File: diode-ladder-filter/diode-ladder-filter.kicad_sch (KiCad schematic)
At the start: 67 parts, among them J1 Input, J2 CV1, J3 CV2, J4 Output, J5 Power, J6 Power, J7 Power, SW1 LPF, SW2 Resonance_safety, SW3 BPF, SW4 HPF, U1 TL074, U2 TL074

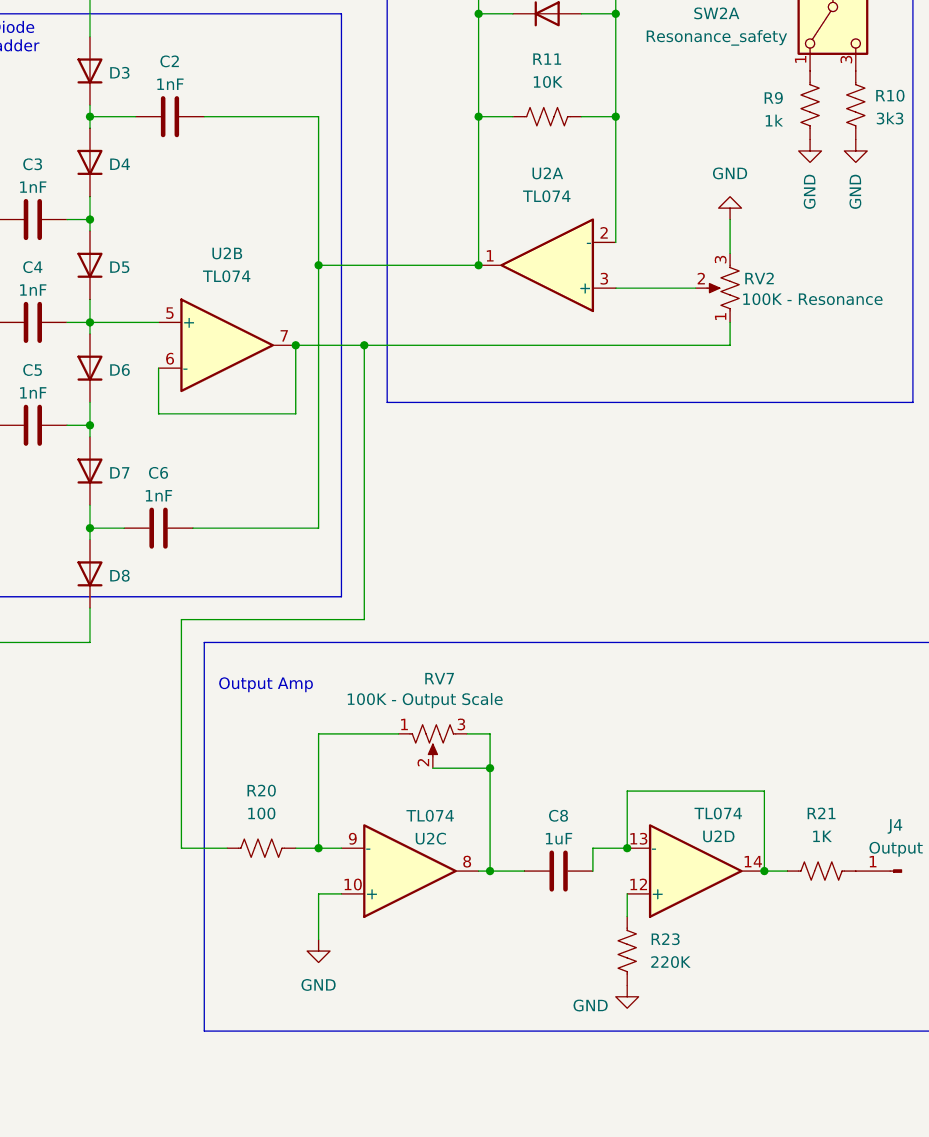
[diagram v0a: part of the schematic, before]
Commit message: Update diode ladder
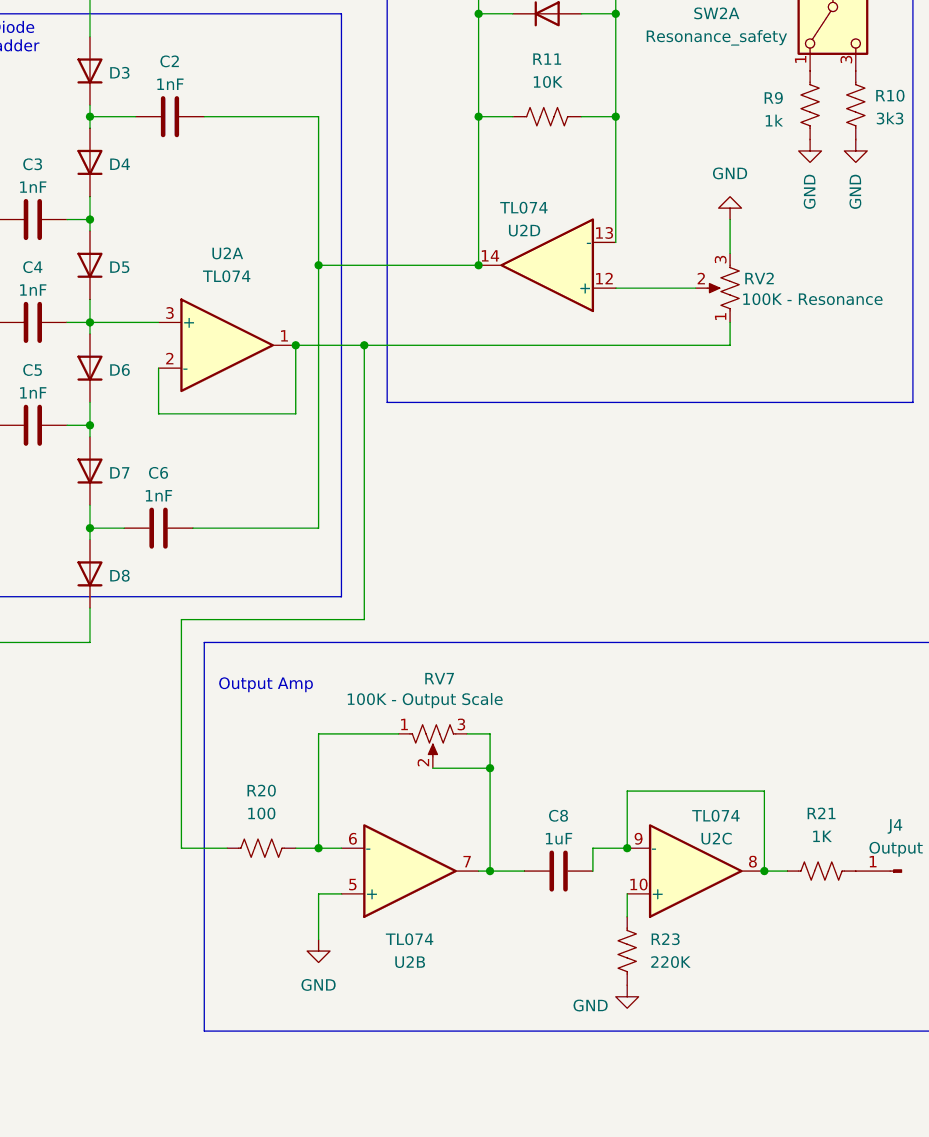
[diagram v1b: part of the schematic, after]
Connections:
- net GND: now also U2.5 (+); no longer U2.10 (+)
- net at C8.1, RV7.2, RV7.3: now also U2.7; no longer U2.8
- net at C8.2, R21.1: now also U2.8, U2.9 (-); no longer U2.13 (-), U2.14
- net at C2.2, C6.2, D1.2 (A)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: now also U2.14; no longer U2.1
- net at D1.1 (K), D2.2 (A), R11.2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: now also U2.13 (-); no longer U2.2 (-)
- net at U2.3 (+): now also C4.2, D5.1 (K), D6.2 (A); no longer RV2.2
- net at R20.2, RV7.1: now also U2.6 (-); no longer U2.9 (-)
- net at R20.1, RV2.1: now also U2.1, U2.2 (-); no longer U2.6 (-), U2.7
- net at U2.12 (+): now also RV2.2; no longer R23.1
- new net: R23.1, U2.10 (+)

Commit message: Update some modules
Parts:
- added J10: Input, modular2:banana-jack, symbol Connector:Conn_01x01_Pin
- added J11: Output, modular2:banana-jack, symbol Connector:Conn_01x01_Pin
- added J12: Conn_01x04_Socket, Connector_PinSocket_2.54mm:PinSocket_1x04_P2.54mm_Vertical, symbol Connector:Conn_01x04_Socket
- added J13: Conn_01x04_Pin, Connector_PinHeader_2.54mm:PinHeader_1x04_P2.54mm_Vertical, symbol Connector:Conn_01x04_Pin
- added J8: CV1, modular2:banana-jack, symbol Connector:Conn_01x01_Pin
- added J9: CV2, modular2:banana-jack, symbol Connector:Conn_01x01_Pin
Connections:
- net at J3.1 (Pin_1), RV4.3: now also J12.2 (Pin_2)
- net at J4.1 (Pin_1), R21.2: now also J12.4 (Pin_4)
- net at J2.1 (Pin_1), RV3.3: now also J12.1 (Pin_1)
- net at J1.1 (Pin_1), RV1.3: now also J12.3 (Pin_3)
- new net: J10.1 (Pin_1), J13.3 (Pin_3)
- new net: J13.1 (Pin_1), J8.1 (Pin_1)
- new net: J11.1 (Pin_1), J13.4 (Pin_4)
- new net: J13.2 (Pin_2), J9.1 (Pin_1)

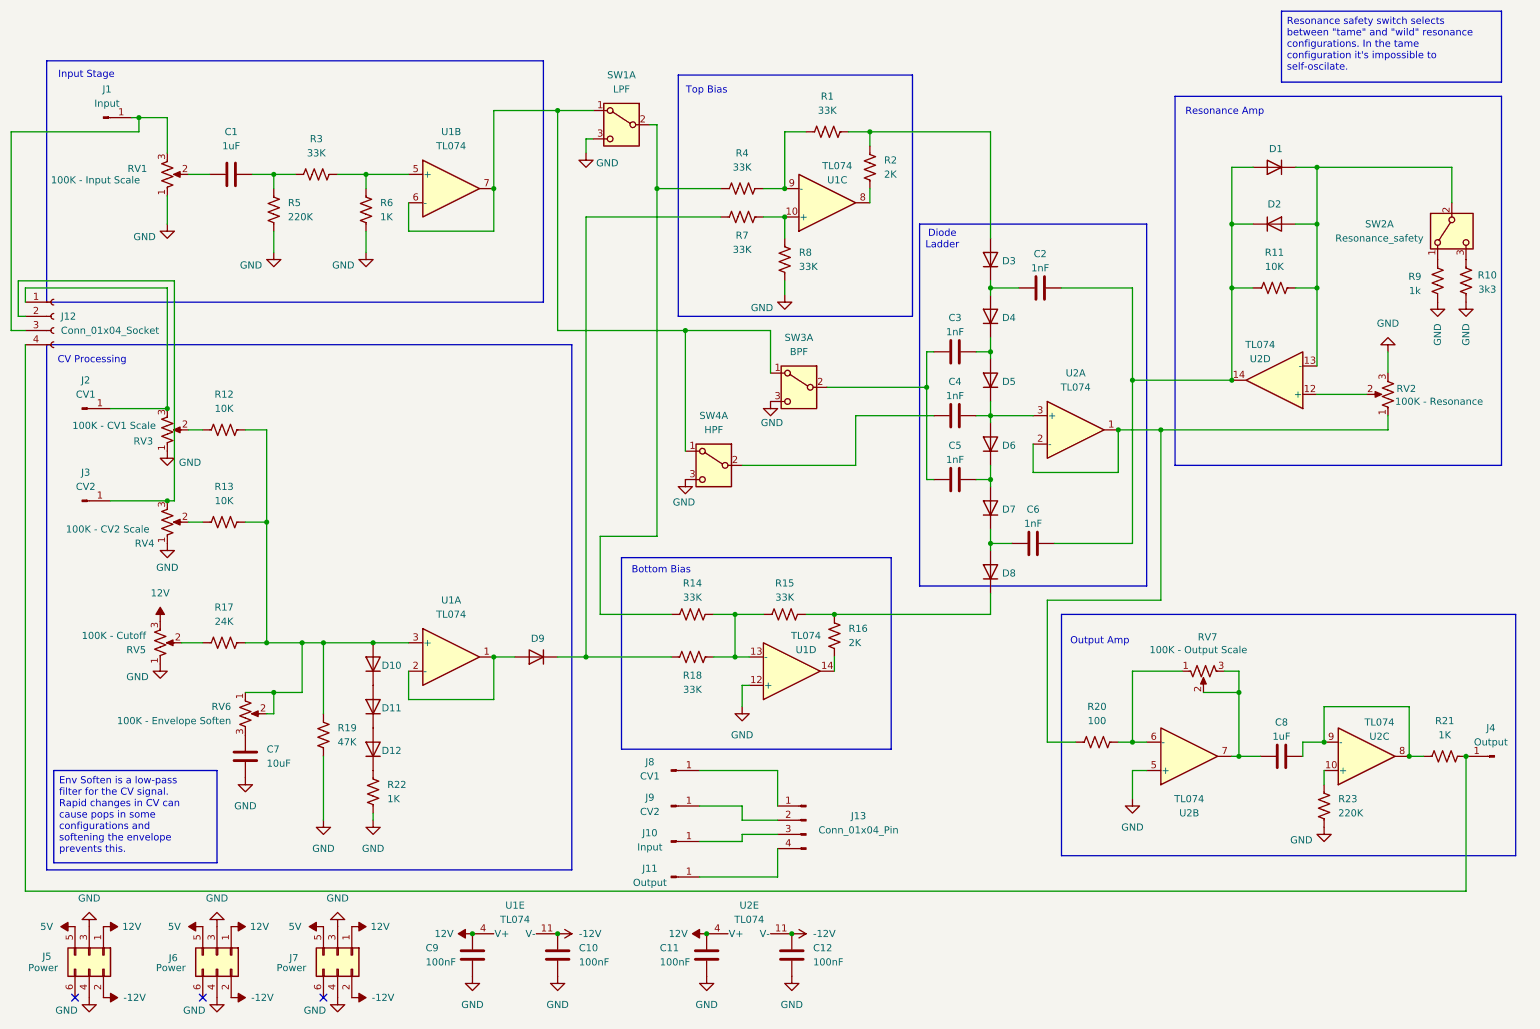
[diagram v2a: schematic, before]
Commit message: Start fixing issues with diode ladder
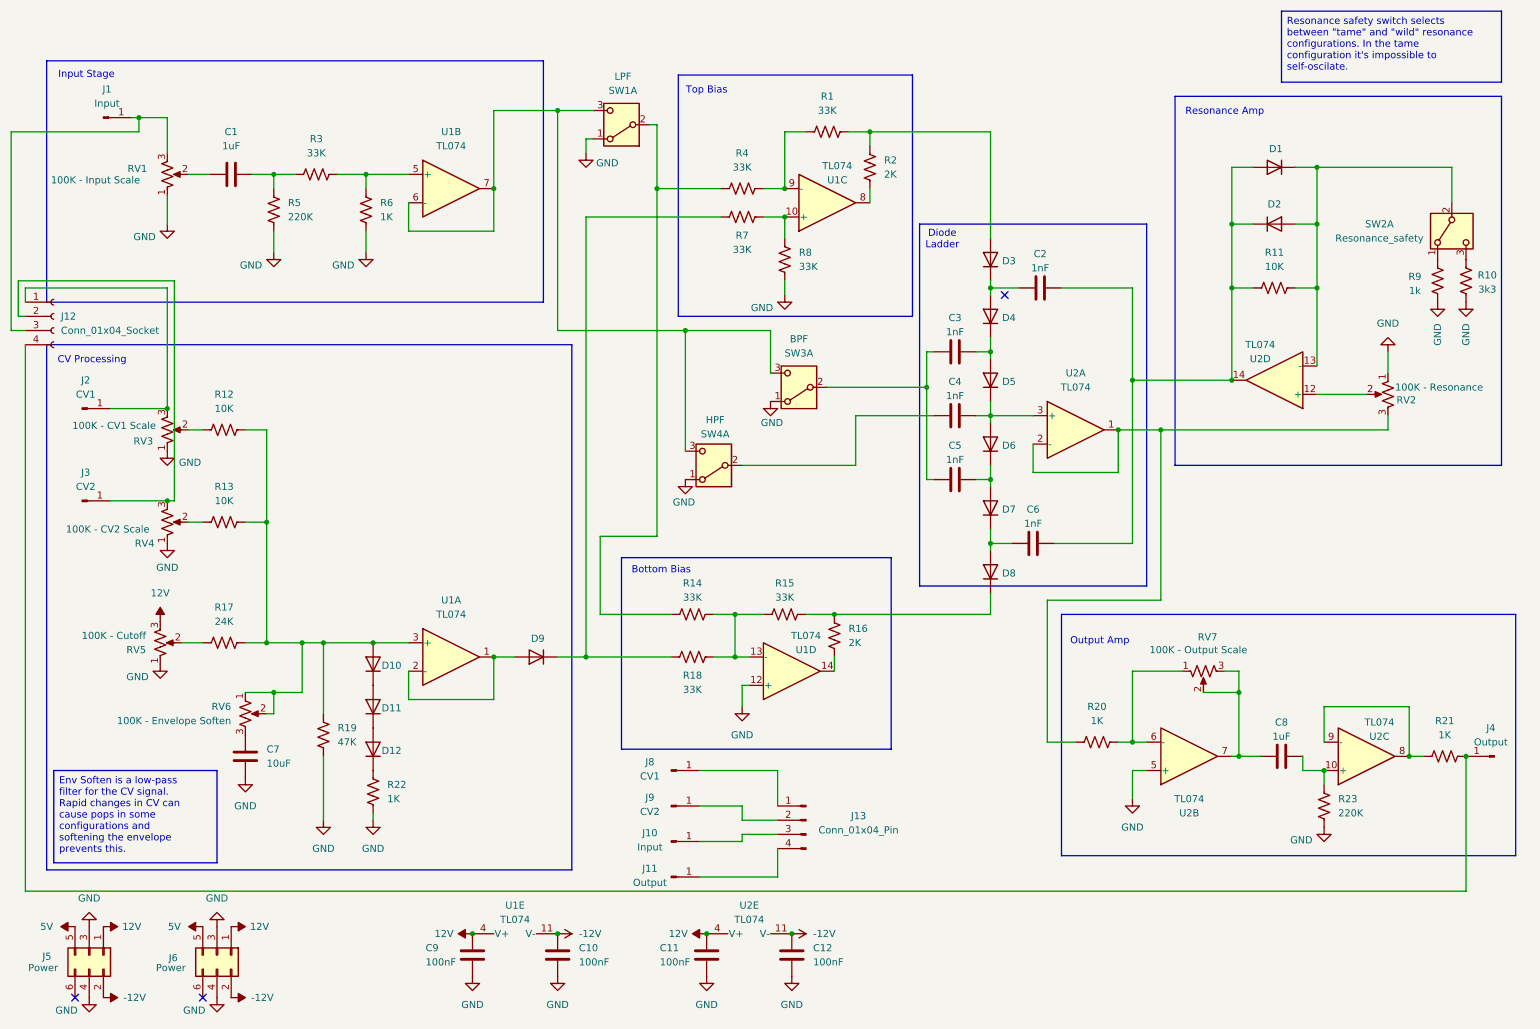
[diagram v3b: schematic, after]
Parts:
- removed J7: Power, Connector_IDC:IDC-Header_2x03_P2.54mm_Vertical, symbol Connector_Generic:Conn_02x03_Odd_Even
- R20: value 100 -> 1K
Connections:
- net GND: now also RV2.1, SW1.1 (A), SW3.1 (A), SW4.1 (A); no longer RV2.3, SW1.3 (C), SW3.3 (C), SW4.3 (C)
- net at R21.1, U2.8, U2.9 (-): no longer C8.2
- net at R20.1, U2.1, U2.2 (-): now also RV2.3; no longer RV2.1
- net at R23.1, U2.10 (+): now also C8.2
- new net: SW1.3 (C), SW3.3 (C), SW4.3 (C), U1.6 (-), U1.7
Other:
- moved on the sheet: RV2, SW1A, SW3A, SW4A

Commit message: Renumber some components
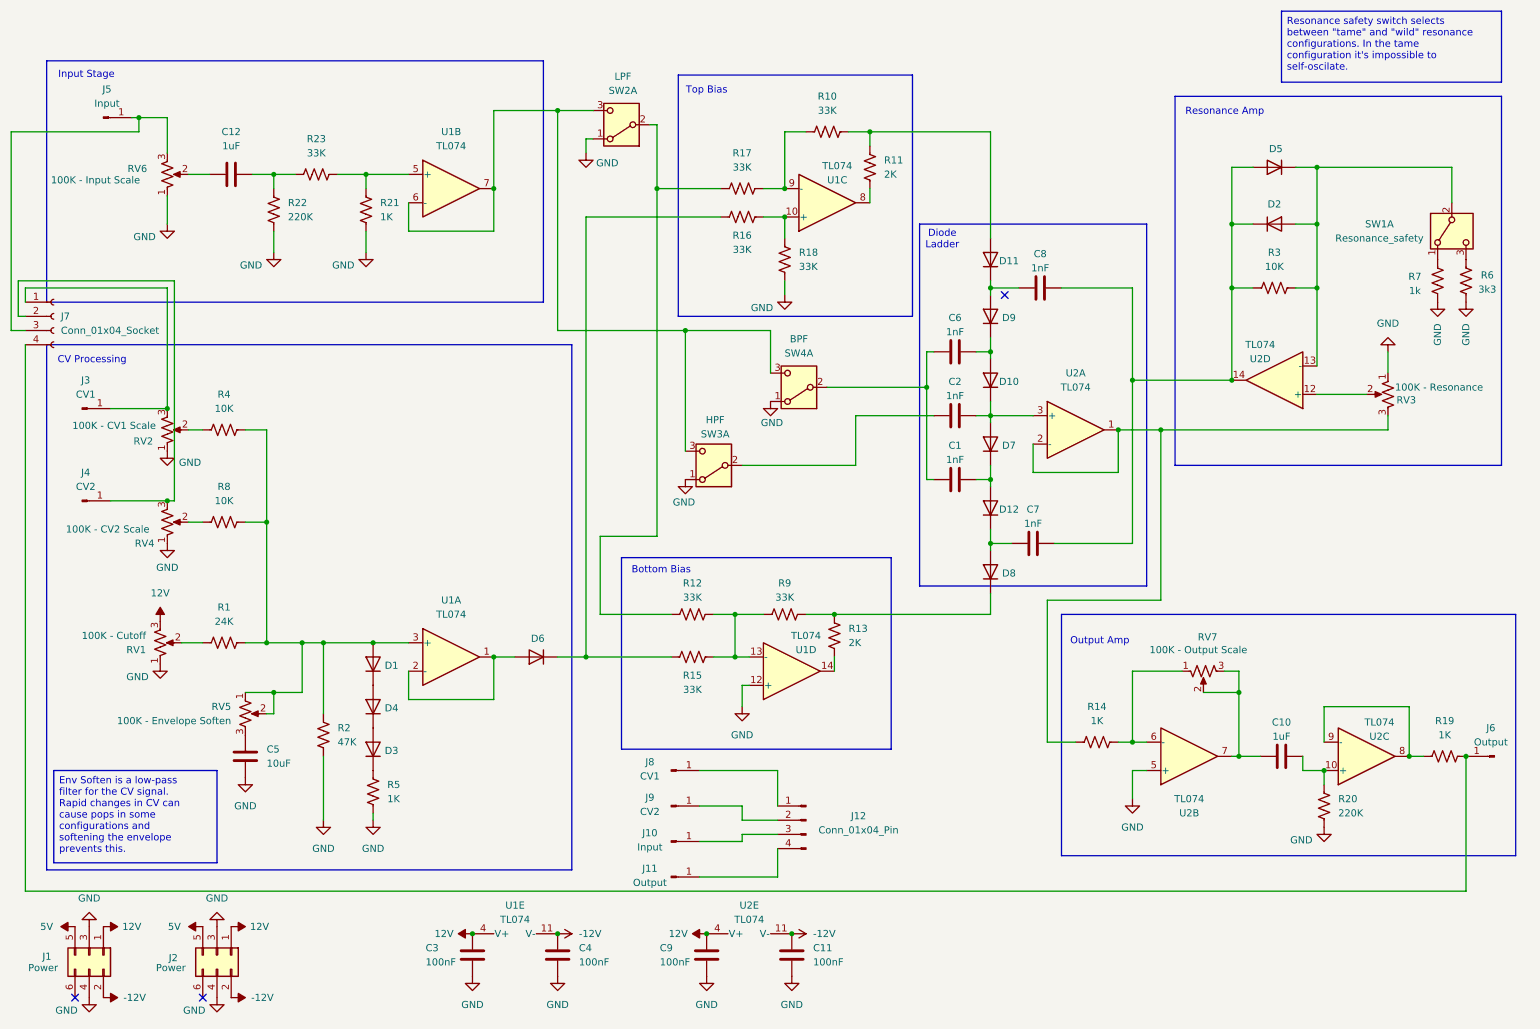
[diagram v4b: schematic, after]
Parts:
- renumbered C5 to C1, C8 to C10, C12 to C11, C1 to C12, C4 to C2, C9 to C3, C10 to C4, C7 to C5, C3 to C6, C6 to C7, C2 to C8, C11 to C9, D10 to D1, D5 to D10, D3 to D11, D7 to D12, D12 to D3, D11 to D4, D1 to D5, D9 to D6, D6 to D7, D4 to D9, J5 to J1, J13 to J12, J6 to J2, J2 to J3, J3 to J4, J1 to J5, J4 to J6, J12 to J7, R17 to R1, R1 to R10, R2 to R11, R14 to R12, R16 to R13, R20 to R14, R18 to R15, R7 to R16, R4 to R17, R8 to R18, R21 to R19, R19 to R2, R23 to R20, R6 to R21, R5 to R22, R3 to R23, R11 to R3, R12 to R4, R22 to R5, R10 to R6, R9 to R7, R13 to R8, R15 to R9, RV5 to RV1, RV3 to RV2, RV2 to RV3, RV6 to RV5, RV1 to RV6, SW2 to SW1, SW1 to SW2, SW4 to SW3, SW3 to SW4
